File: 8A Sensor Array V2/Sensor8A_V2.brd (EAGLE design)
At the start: 107.7 x 25.1 mm, 27 parts, among them T1 2N2222

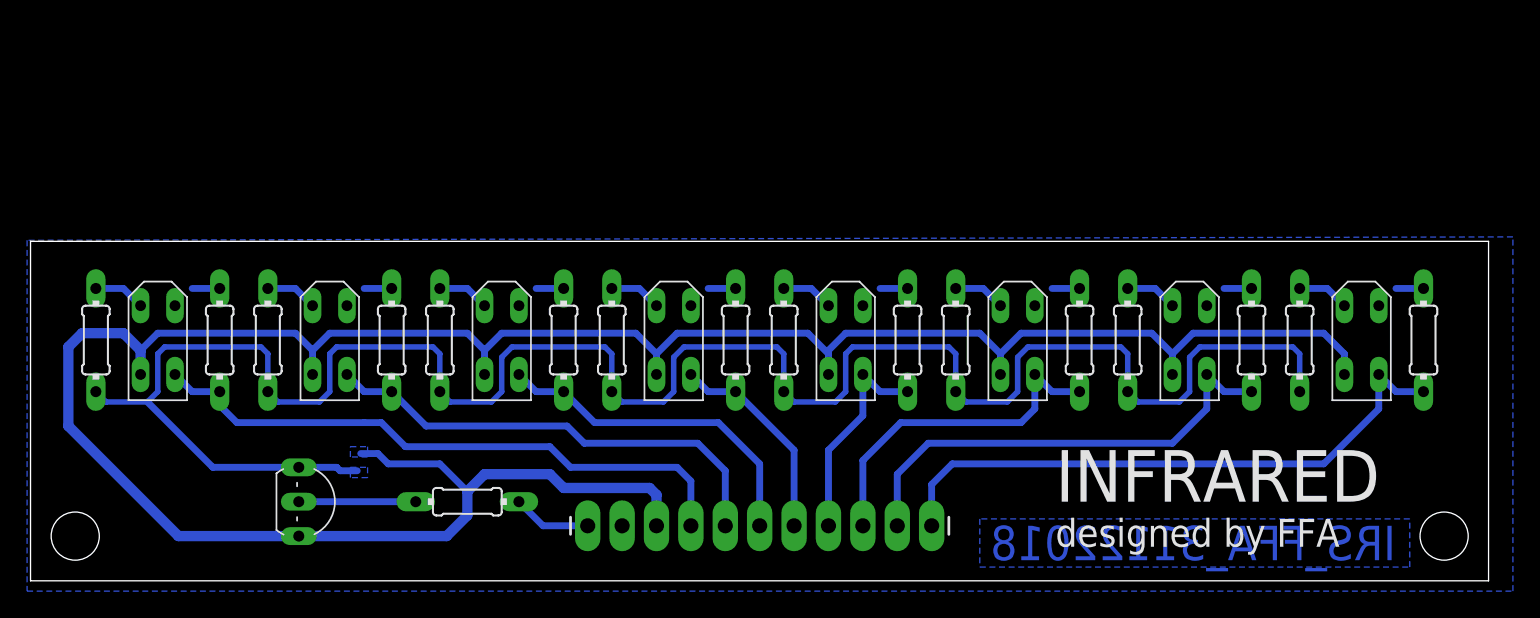
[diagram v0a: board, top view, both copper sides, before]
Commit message: V1 updated and V2 added
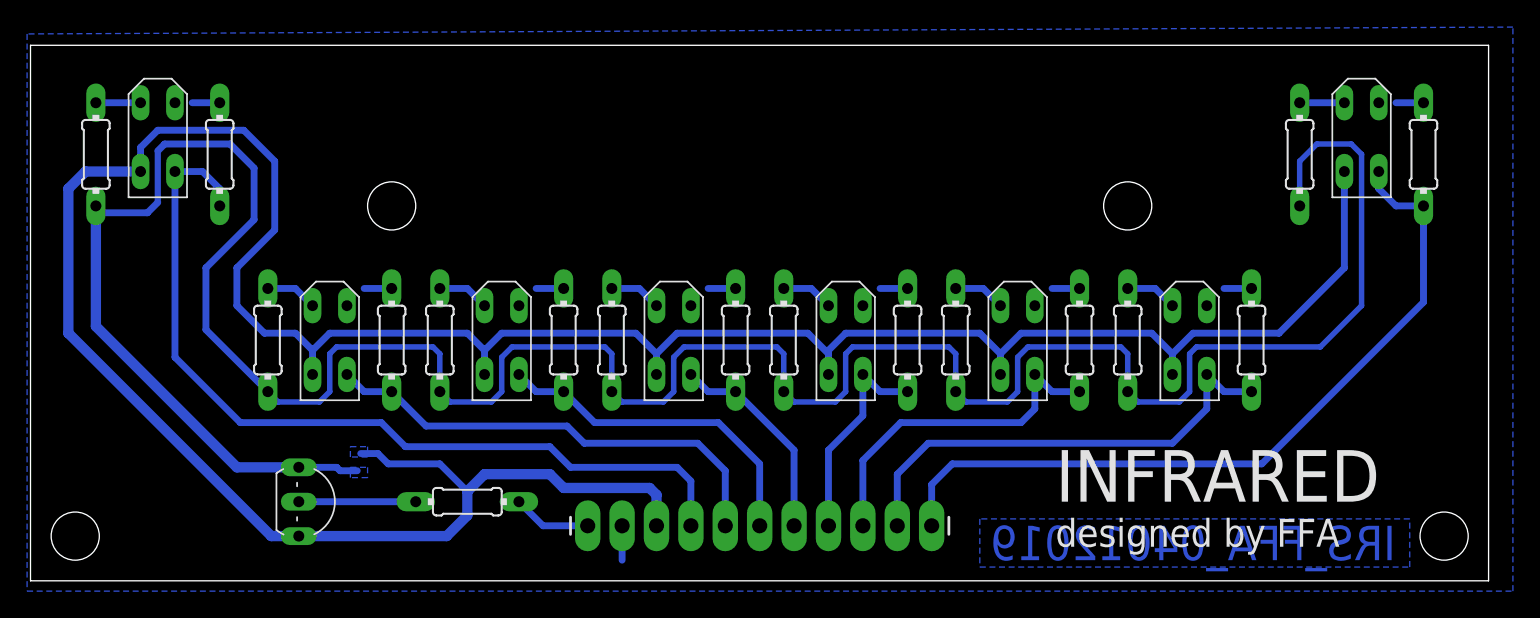
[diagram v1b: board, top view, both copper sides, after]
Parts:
- moved OS1 15.0 mm to (9.40, 32.8)
- moved OS8 15.0 mm to (98.3, 32.8)
- moved R1 13.7 mm to (4.83, 31.5)
- moved R16 13.7 mm to (93.7, 31.5)
- moved R17 13.7 mm to (102.9, 31.5)
- moved R2 13.7 mm to (14.0, 31.5)
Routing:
- net LED: track 152.4 -> 207.8 mm
- net VCC: track 184.1 -> 214.7 mm
- net S1: track 45.3 -> 64.0 mm
- net S8: track 44.8 -> 57.2 mm
- net GND: track 16.3 -> 18.8 mm
- net N$1: track 3.83 -> 3.30 mm
- net N$8: track 3.83 -> 3.30 mm
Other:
- board size 107.7 x 25.1 mm -> 107.7 x 39.5 mm
- board text added: "IRS_FFA_04012019"
- board text removed: "IRS_FFA_31122018"
